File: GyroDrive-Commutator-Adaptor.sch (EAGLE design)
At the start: 24 parts, among them U1 HALL, U2 PCA9517, U3 5V, U4 2.5V, U5 INA2141U, U6 INA2141U, U7 INA2141U, X1 NORCOMP-DB25-SMD-MALE

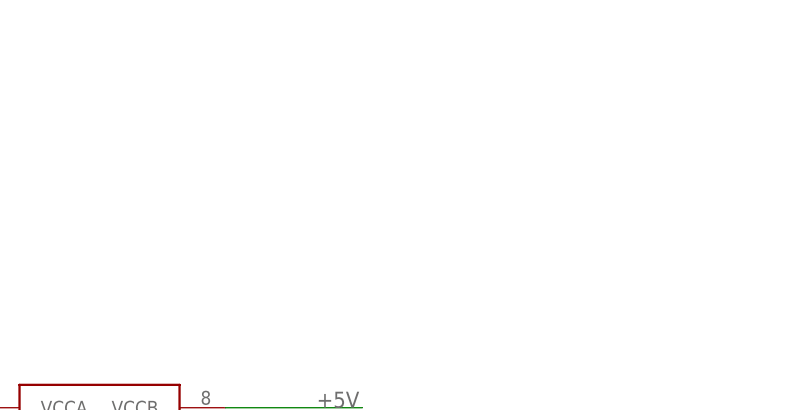
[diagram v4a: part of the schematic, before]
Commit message: I2C pull-up resistors added
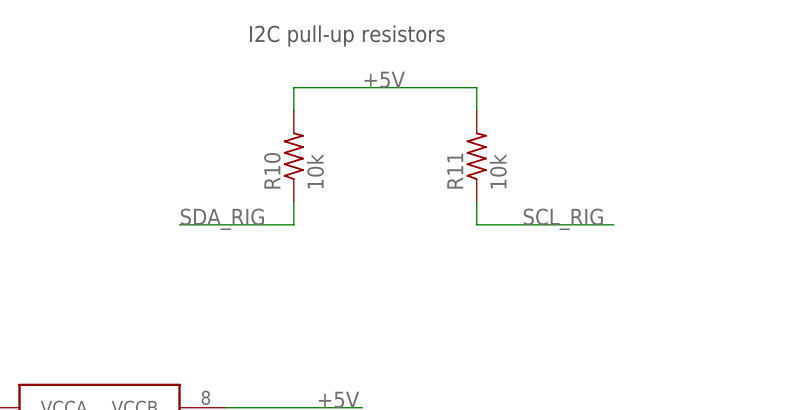
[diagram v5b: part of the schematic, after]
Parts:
- added R10, R11: 10k, resistor:R-US_R0402
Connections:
- net +5V: now also R10.2, R11.2
- net SCL_RIG: now also R11.1
- net SDA_RIG: now also R10.1
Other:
- note added: "I2C pull-up resistors"
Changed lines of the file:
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@@
 <part name="C2" library="resistor" deviceset="C-US" device="C0402"/>
 <part name="C4" library="resistor" deviceset="C-US" device="C0402"/>
+<part name="R10" library="resistor" deviceset="R-US_" device="R0402" value="10k"/>
+<part name="R11" library="resistor" deviceset="R-US_" device="R0402" value="10k"/>
 </parts>
 <sheets>
@@
 sense to Vo, and
 leave Ref open-circuit."</text>
+<text x="-121.92" y="363.22" size="1.778" layer="97">I2C pull-up resistors</text>
 </plain>
 <instances>
@@
 <instance part="C2" gate="G$1" x="-210.82" y="345.44"/>
 <instance part="C4" gate="G$1" x="-185.42" y="345.44"/>
+<instance part="R10" gate="G$1" x="-116.84" y="350.52" rot="R90"/>
+<instance part="R11" gate="G$1" x="-96.52" y="350.52" rot="R90"/>
 </instances>
 <busses>
@@
 <label x="-177.8" y="320.04" size="1.778" layer="95"/>
 </segment>
+<segment>
+<wire x1="-116.84" y1="355.6" x2="-116.84" y2="358.14" width="0.1524" layer="91"/>
+<wire x1="-116.84" y1="358.14" x2="-96.52" y2="358.14" width="0.1524" layer="91"/>
+<wire x1="-96.52" y1="358.14" x2="-96.52" y2="355.6" width="0.1524" layer="91"/>
+<label x="-109.22" y="358.14" size="1.778" layer="95"/>
+<pinref part="R10" gate="G$1" pin="2"/>
+<pinref part="R11" gate="G$1" pin="2"/>
+</segment>
 </net>
 <net name="SDA_BIRD" class="0">
@@
 <label x="-93.98" y="256.54" size="1.778" layer="95"/>
 </segment>
+<segment>
+<wire x1="-116.84" y1="345.44" x2="-116.84" y2="342.9" width="0.1524" layer="91"/>
+<wire x1="-116.84" y1="342.9" x2="-129.54" y2="342.9" width="0.1524" layer="91"/>
+<label x="-129.54" y="342.9" size="1.778" layer="95"/>
+<pinref part="R10" gate="G$1" pin="1"/>
+</segment>
 </net>
 <net name="SCL_RIG" class="0">
@@
 <label x="-93.98" y="254" size="1.778" layer="95"/>
 </segment>
-</net>
+<segment>
+<wire x1="-96.52" y1="345.44" x2="-96.52" y2="342.9" width="0.1524" layer="91"/>
+<wire x1="-96.52" y1="342.9" x2="-81.28" y2="342.9" width="0.1524" layer="91"/>
+<label x="-91.44" y="342.9" size="1.778" layer="95"/>
+<pinref part="R11" gate="G$1" pin="1"/>
+</segment>
+</net>

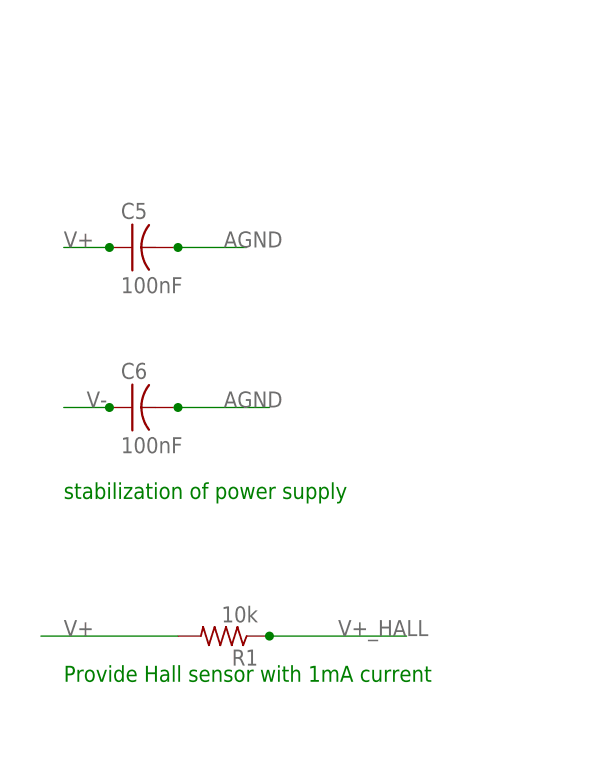
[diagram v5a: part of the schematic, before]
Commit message: Fixed stop mask DRC errors on some resistors and capacitors
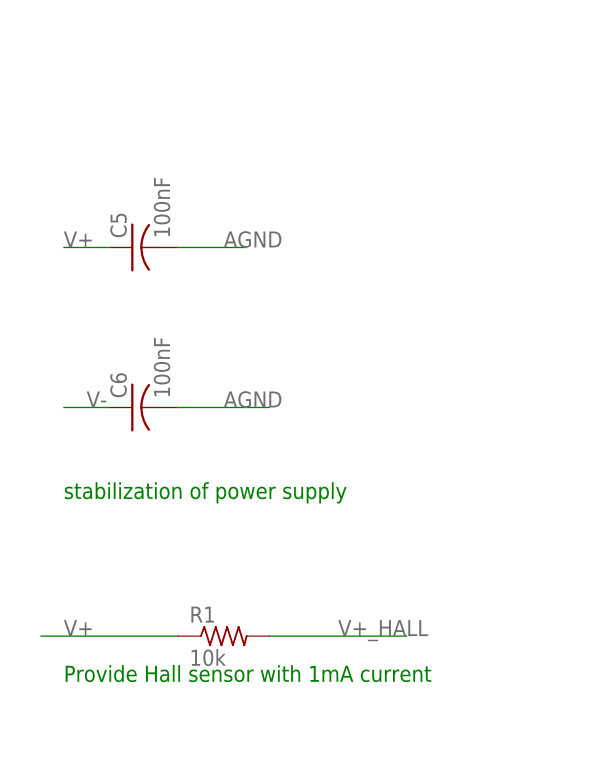
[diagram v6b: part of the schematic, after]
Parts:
- C5, C6: device elm:C0805ELM -> resistor:C-USC0805
- R1: device elm:R0805ELM -> resistor:R-US_R0805
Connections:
- net V+: now also R1.1; no longer R1.2
- net V+_HALL: now also R1.2; no longer R1.1
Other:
- moved on the sheet: R1
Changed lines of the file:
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@@
 <part name="U5" library="burr-brown" deviceset="INA2141" device="U"/>
 <part name="U6" library="burr-brown" deviceset="INA2141" device="U"/>
-<part name="R1" library="elm" deviceset="R0805ELM" device="" value="10k"/>
-<part name="C5" library="elm" deviceset="C0805ELM" device="" value="100nF"/>
-<part name="C6" library="elm" deviceset="C0805ELM" device="" value="100nF"/>
 <part name="X2" library="pinhead" deviceset="PINHD-2X8" device=""/>
 <part name="U1" library="elm" deviceset="HALL_ON_SIDE" device="" value="HALL"/>
@@
 <part name="R10" library="resistor" deviceset="R-US_" device="R0402" value="10k"/>
 <part name="R11" library="resistor" deviceset="R-US_" device="R0402" value="10k"/>
+<part name="R1" library="resistor" deviceset="R-US_" device="R0805" value="10k"/>
+<part name="C5" library="resistor" deviceset="C-US" device="C0805" value="100nF"/>
+<part name="C6" library="resistor" deviceset="C-US" device="C0805" value="100nF"/>
 </parts>
 <sheets>
@@
 <instance part="U5" gate="G$1" x="-71.12" y="180.34"/>
 <instance part="U6" gate="G$1" x="-73.66" y="116.84"/>
-<instance part="R1" gate="G$1" x="-203.2" y="38.1" rot="R180"/>
-<instance part="C5" gate="G$1" x="-213.36" y="81.28"/>
-<instance part="C6" gate="G$1" x="-213.36" y="63.5"/>
 <instance part="X2" gate="A" x="-195.58" y="205.74"/>
 <instance part="U1" gate="G$1" x="-193.04" y="172.72"/>
@@
 <instance part="R10" gate="G$1" x="-116.84" y="350.52" rot="R90"/>
 <instance part="R11" gate="G$1" x="-96.52" y="350.52" rot="R90"/>
+<instance part="R1" gate="G$1" x="-203.2" y="38.1"/>
+<instance part="C5" gate="G$1" x="-213.36" y="81.28" rot="R90"/>
+<instance part="C6" gate="G$1" x="-213.36" y="63.5" rot="R90"/>
 </instances>
 <busses>
@@
 <net name="V-" class="0">
 <segment>
-<pinref part="C6" gate="G$1" pin="1"/>
 <wire x1="-215.9" y1="63.5" x2="-220.98" y2="63.5" width="0.1524" layer="91"/>
 <label x="-218.44" y="63.5" size="1.778" layer="95"/>
-<junction x="-215.9" y="63.5"/>
+<pinref part="C6" gate="G$1" pin="1"/>
 </segment>
 <segment>
@@
 <segment>
 <wire x1="-223.52" y1="38.1" x2="-208.28" y2="38.1" width="0.1524" layer="91"/>
-<pinref part="R1" gate="G$1" pin="2"/>
 <label x="-220.98" y="38.1" size="1.778" layer="95"/>
-</segment>
-<segment>
-<pinref part="C5" gate="G$1" pin="1"/>
+<pinref part="R1" gate="G$1" pin="1"/>
+</segment>
+<segment>
 <wire x1="-215.9" y1="81.28" x2="-220.98" y2="81.28" width="0.1524" layer="91"/>
 <label x="-220.98" y="81.28" size="1.778" layer="95"/>
-<junction x="-215.9" y="81.28"/>
+<pinref part="C5" gate="G$1" pin="1"/>
 </segment>
 <segment>
@@
 <net name="V+_HALL" class="0">
 <segment>
-<pinref part="R1" gate="G$1" pin="1"/>
 <wire x1="-198.12" y1="38.1" x2="-182.88" y2="38.1" width="0.1524" layer="91"/>
 <label x="-190.5" y="38.1" size="1.778" layer="95"/>
-<junction x="-198.12" y="38.1"/>
+<pinref part="R1" gate="G$1" pin="2"/>
 </segment>
 <segment>
@@
 </segment>
 <segment>
-<pinref part="C5" gate="G$1" pin="2"/>
 <wire x1="-208.28" y1="81.28" x2="-200.66" y2="81.28" width="0.1524" layer="91"/>
 <label x="-203.2" y="81.28" size="1.778" layer="95"/>
-<junction x="-208.28" y="81.28"/>
-</segment>
-<segment>
-<pinref part="C6" gate="G$1" pin="2"/>
+<pinref part="C5" gate="G$1" pin="2"/>
+</segment>
+<segment>
 <wire x1="-208.28" y1="63.5" x2="-198.12" y2="63.5" width="0.1524" layer="91"/>
 <label x="-203.2" y="63.5" size="1.778" layer="95"/>
-<junction x="-208.28" y="63.5"/>
-</segment>
-<segment>
+<pinref part="C6" gate="G$1" pin="2"/>
+</segment>
+<segment>

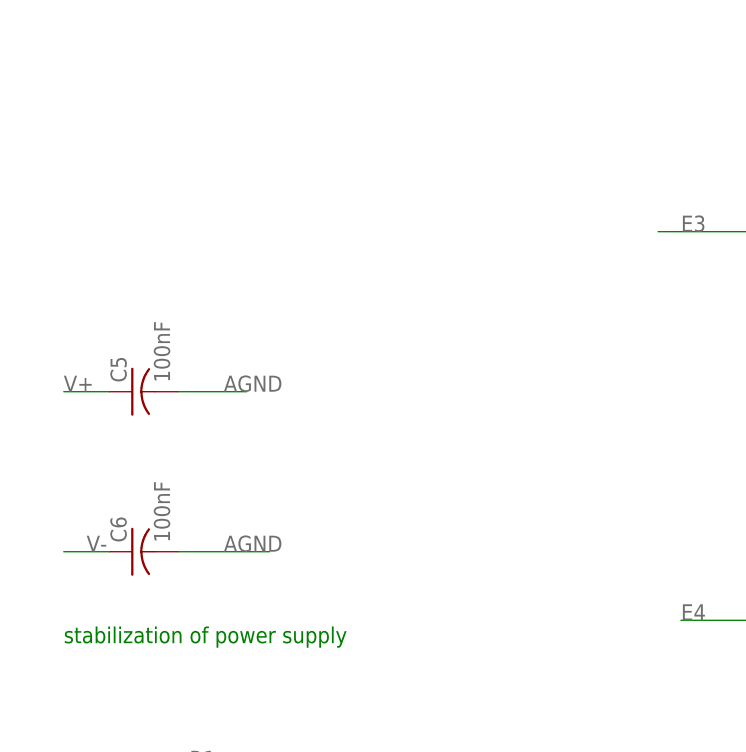
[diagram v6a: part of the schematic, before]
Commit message: Added more bypass capacitors (one for each power supply on each instrumentation amp)
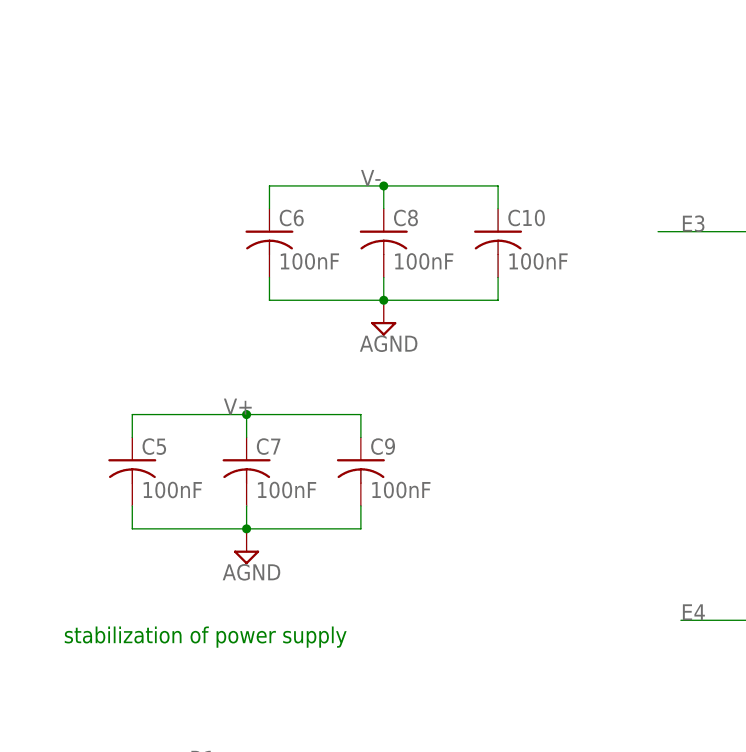
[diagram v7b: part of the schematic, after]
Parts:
- added C10, C7, C8, C9: 100nF, resistor:C-USC0805
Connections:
- net AGND: now also C10.2, C7.2, C8.2, C9.2
- net V+: now also C7.1, C9.1
- net V-: now also C10.1, C8.1
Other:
- moved on the sheet: C5, C6
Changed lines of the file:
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@@
 <?xml version="1.0" encoding="utf-8"?>
 <!DOCTYPE eagle SYSTEM "eagle.dtd">
-<eagle version="7.4.0">
+<eagle version="7.5.0">
 <drawing>
 <settings>
@@
 <part name="C5" library="resistor" deviceset="C-US" device="C0805" value="100nF"/>
 <part name="C6" library="resistor" deviceset="C-US" device="C0805" value="100nF"/>
+<part name="C7" library="resistor" deviceset="C-US" device="C0805" value="100nF"/>
+<part name="C8" library="resistor" deviceset="C-US" device="C0805" value="100nF"/>
+<part name="C9" library="resistor" deviceset="C-US" device="C0805" value="100nF"/>
+<part name="C10" library="resistor" deviceset="C-US" device="C0805" value="100nF"/>
+<part name="SUPPLY5" library="supply2" deviceset="AGND" device=""/>
+<part name="SUPPLY7" library="supply2" deviceset="AGND" device=""/>
 </parts>
 <sheets>
@@
 <instance part="R11" gate="G$1" x="-96.52" y="350.52" rot="R90"/>
 <instance part="R1" gate="G$1" x="-203.2" y="38.1"/>
-<instance part="C5" gate="G$1" x="-213.36" y="81.28" rot="R90"/>
-<instance part="C6" gate="G$1" x="-213.36" y="63.5" rot="R90"/>
+<instance part="C5" gate="G$1" x="-213.36" y="73.66"/>
+<instance part="C6" gate="G$1" x="-198.12" y="99.06"/>
+<instance part="C7" gate="G$1" x="-200.66" y="73.66"/>
+<instance part="C8" gate="G$1" x="-185.42" y="99.06"/>
+<instance part="C9" gate="G$1" x="-187.96" y="73.66"/>
+<instance part="C10" gate="G$1" x="-172.72" y="99.06"/>
+<instance part="SUPPLY5" gate="G$1" x="-185.42" y="88.9"/>
+<instance part="SUPPLY7" gate="G$1" x="-200.66" y="63.5"/>
 </instances>
 <busses>
@@
 <net name="V-" class="0">
 <segment>
-<wire x1="-215.9" y1="63.5" x2="-220.98" y2="63.5" width="0.1524" layer="91"/>
-<label x="-218.44" y="63.5" size="1.778" layer="95"/>
-<pinref part="C6" gate="G$1" pin="1"/>
-</segment>
-<segment>
 <label x="-45.72" y="93.98" size="1.778" layer="95"/>
 <wire x1="-58.42" y1="93.98" x2="-55.88" y2="93.98" width="0.1524" layer="91"/>
@@
 <label x="-218.44" y="205.74" size="1.778" layer="95"/>
 </segment>
+<segment>
+<pinref part="C6" gate="G$1" pin="1"/>
+<wire x1="-198.12" y1="101.6" x2="-198.12" y2="104.14" width="0.1524" layer="91"/>
+<wire x1="-198.12" y1="104.14" x2="-185.42" y2="104.14" width="0.1524" layer="91"/>
+<label x="-187.96" y="104.14" size="1.778" layer="95"/>
+<pinref part="C8" gate="G$1" pin="1"/>
+<wire x1="-185.42" y1="104.14" x2="-172.72" y2="104.14" width="0.1524" layer="91"/>
+<wire x1="-185.42" y1="101.6" x2="-185.42" y2="104.14" width="0.1524" layer="91"/>
+<junction x="-185.42" y="104.14"/>
+<pinref part="C10" gate="G$1" pin="1"/>
+<wire x1="-172.72" y1="104.14" x2="-172.72" y2="101.6" width="0.1524" layer="91"/>
+</segment>
 </net>
 <net name="V+" class="0">
@@
 <label x="-220.98" y="38.1" size="1.778" layer="95"/>
 <pinref part="R1" gate="G$1" pin="1"/>
-</segment>
-<segment>
-<wire x1="-215.9" y1="81.28" x2="-220.98" y2="81.28" width="0.1524" layer="91"/>
-<label x="-220.98" y="81.28" size="1.778" layer="95"/>
-<pinref part="C5" gate="G$1" pin="1"/>
 </segment>
 <segment>
@@
 <wire x1="-198.12" y1="203.2" x2="-218.44" y2="203.2" width="0.1524" layer="91"/>
 <label x="-218.44" y="203.2" size="1.778" layer="95"/>
+</segment>
+<segment>
+<pinref part="C5" gate="G$1" pin="1"/>
+<wire x1="-213.36" y1="76.2" x2="-213.36" y2="78.74" width="0.1524" layer="91"/>
+<wire x1="-213.36" y1="78.74" x2="-200.66" y2="78.74" width="0.1524" layer="91"/>
+<wire x1="-200.66" y1="78.74" x2="-187.96" y2="78.74" width="0.1524" layer="91"/>
+<pinref part="C7" gate="G$1" pin="1"/>
+<wire x1="-200.66" y1="76.2" x2="-200.66" y2="78.74" width="0.1524" layer="91"/>
+<junction x="-200.66" y="78.74"/>
+<label x="-203.2" y="78.74" size="1.778" layer="95"/>
+<pinref part="C9" gate="G$1" pin="1"/>
+<wire x1="-187.96" y1="76.2" x2="-187.96" y2="78.74" width="0.1524" layer="91"/>
 </segment>
 </net>
@@
 </segment>
 <segment>
-<wire x1="-208.28" y1="81.28" x2="-200.66" y2="81.28" width="0.1524" layer="91"/>
-<label x="-203.2" y="81.28" size="1.778" layer="95"/>
-<pinref part="C5" gate="G$1" pin="2"/>
-</segment>
-<segment>
-<wire x1="-208.28" y1="63.5" x2="-198.12" y2="63.5" width="0.1524" layer="91"/>
-<label x="-203.2" y="63.5" size="1.778" layer="95"/>
-<pinref part="C6" gate="G$1" pin="2"/>
-</segment>
-<segment>
 <wire x1="-220.98" y1="177.8" x2="-205.74" y2="177.8" width="0.1524" layer="91"/>
 <pinref part="U1" gate="G$1" pin="A"/>
@@
 <label x="-170.18" y="203.2" size="1.778" layer="95" rot="MR0"/>
 </segment>
-</net>
+<segment>
+<pinref part="C6" gate="G$1" pin="2"/>
+<wire x1="-198.12" y1="93.98" x2="-198.12" y2="91.44" width="0.1524" layer="91"/>
+<wire x1="-198.12" y1="91.44" x2="-185.42" y2="91.44" width="0.1524" layer="91"/>
+<wire x1="-185.42" y1="91.44" x2="-172.72" y2="91.44" width="0.1524" layer="91"/>
+<junction x="-185.42" y="91.44"/>
+<pinref part="SUPPLY5" gate="G$1" pin="AGND"/>
+<pinref part="C8" gate="G$1" pin="2"/>
+<wire x1="-185.42" y1="91.44" x2="-185.42" y2="93.98" width="0.1524" layer="91"/>
+<pinref part="C10" gate="G$1" pin="2"/>
+<wire x1="-172.72" y1="91.44" x2="-172.72" y2="93.98" width="0.1524" layer="91"/>
+</segment>
+<segment>
+<pinref part="C5" gate="G$1" pin="2"/>
+<wire x1="-213.36" y1="68.58" x2="-213.36" y2="66.04" width="0.1524" layer="91"/>
+<wire x1="-213.36" y1="66.04" x2="-200.66" y2="66.04" width="0.1524" layer="91"/>
+<wire x1="-200.66" y1="66.04" x2="-187.96" y2="66.04" width="0.1524" layer="91"/>
+<pinref part="C7" gate="G$1" pin="2"/>
+<wire x1="-200.66" y1="68.58" x2="-200.66" y2="66.04" width="0.1524" layer="91"/>
+<junction x="-200.66" y="66.04"/>
+<pinref part="SUPPLY7" gate="G$1" pin="AGND"/>
+<pinref part="C9" gate="G$1" pin="2"/>
+<wire x1="-187.96" y1="68.58" x2="-187.96" y2="66.04" width="0.1524" layer="91"/>
+</segment>
+</net>
